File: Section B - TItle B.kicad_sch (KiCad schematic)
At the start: 20 parts, among them J2 CAN1, J5 RJHSE5380, J6 CAN1, U2 MCP2515-xST, U3 ISO1050DUB, U4 ISO1050DUB, Y1 ABM3B-8.000MHZ-10-1-U-T

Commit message: Final Changes, Updated to Checked
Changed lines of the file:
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@@
 		)
 	)
-	(text_box "Block Description"
+	(text_box "CAN1 - Native ESP32"
 		(exclude_from_sim no)
 		(at 129.54 80.01 0)
@@
 		(stroke
 			(width -0.0001)
-			(type default)
+			(type solid)
 		)
 		(fill
@@
 		)
 	)
-	(text_box "Block Description"
+	(text_box "CAN2 - Aux. CAN for Victron"
 		(exclude_from_sim no)
 		(at 129.54 133.35 0)
@@
 		(stroke
 			(width -0.0001)
-			(type default)
+			(type solid)
 		)
 		(fill
@@
 		)
 	)
-	(text_box "Block Description"
+	(text_box "Crystal for CAN"
 		(exclude_from_sim no)
 		(at 238.76 218.44 0)
@@
 		(stroke
 			(width -0.0001)
-			(type default)
+			(type solid)
 		)
 		(fill
@@
 		)
 	)
-	(text_box "Block Description"
+	(text_box "SPI CAN Interface"
 		(exclude_from_sim no)
 		(at 129.54 218.44 0)
@@
 		(stroke
 			(width -0.0001)
-			(type default)
+			(type solid)
 		)
 		(fill

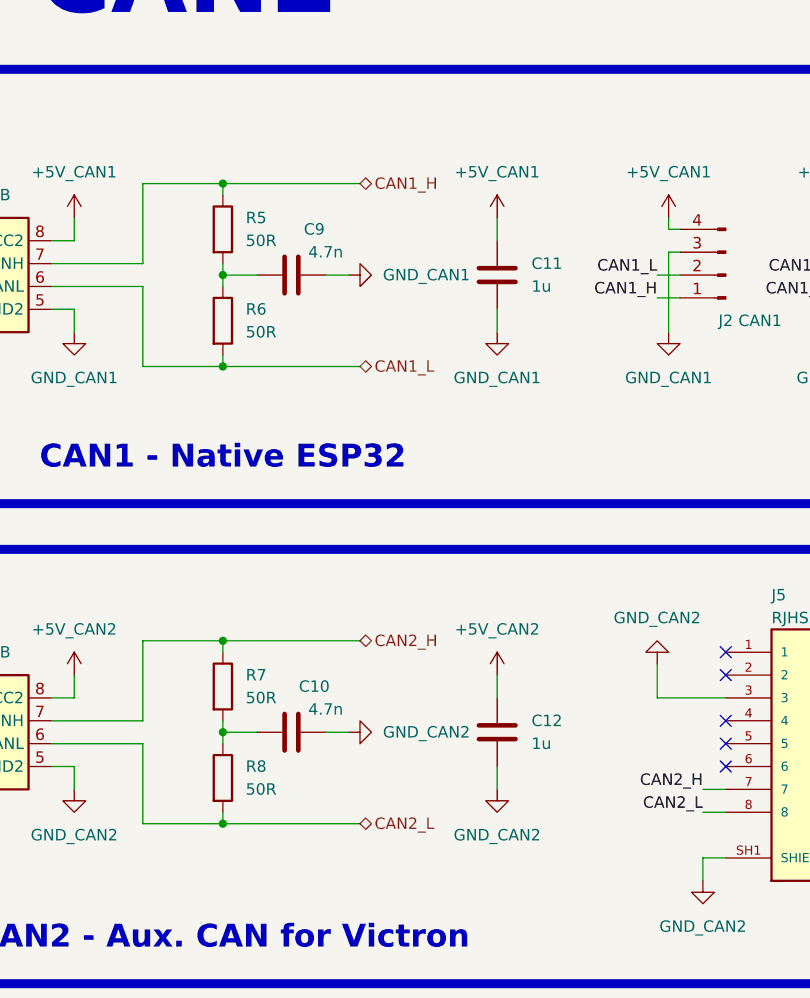
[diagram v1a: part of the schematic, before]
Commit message: Retry with rules DRC ERC passing
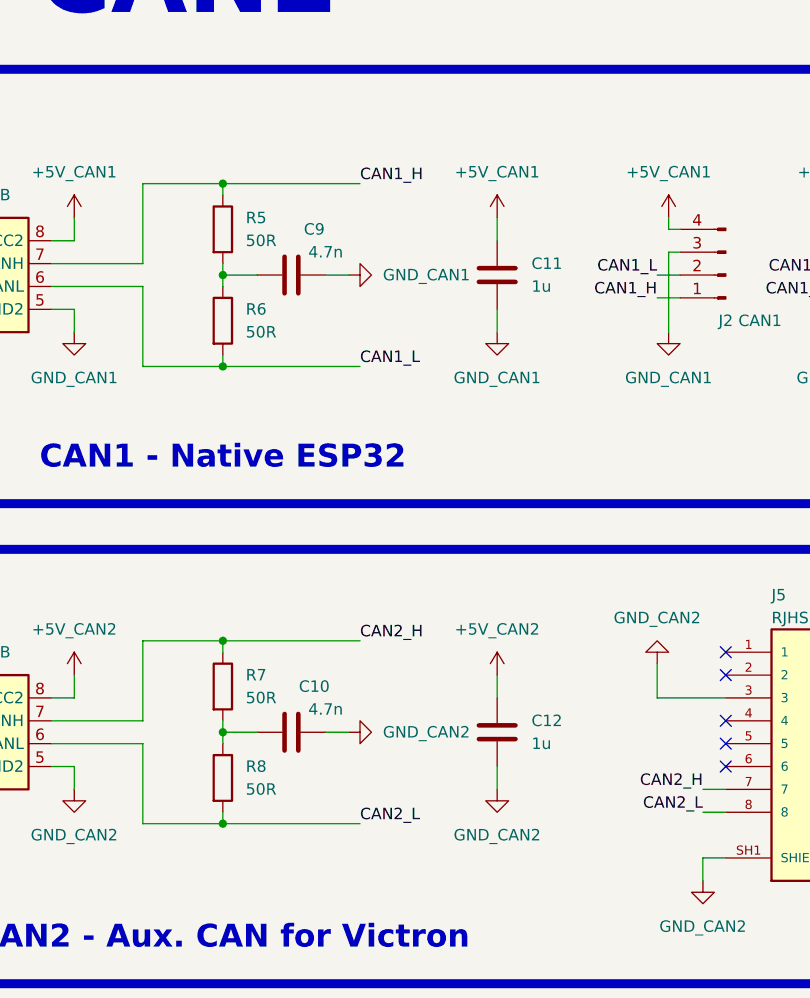
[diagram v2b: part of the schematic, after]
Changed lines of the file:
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@@
+		)
+	)
+	(label "CAN1_L"
+		(at 228.6 76.2 0)
+		(effects
+			(font
+				(size 1.27 1.27)
+			)
+			(justify left bottom)
 		)
 	)
@@
 		)
 	)
+	(label "CAN1_H"
+		(at 228.6 55.88 0)
+		(effects
+			(font
+				(size 1.27 1.27)
+			)
+			(justify left bottom)
+		)
+	)
 	(label "CAN2_H"
 		(at 266.7 123.19 180)
@@
 		)
 	)
+	(label "CAN2_H"
+		(at 228.6 106.68 0)
+		(effects
+			(font
+				(size 1.27 1.27)
+			)
+			(justify left bottom)
+		)
+	)
 	(label "CAN2_L"
 		(at 266.7 125.73 180)
@@
 			)
 			(justify right bottom)
+		)
+	)
+	(label "CAN2_L"
+		(at 228.6 127 0)
+		(effects
+			(font
+				(size 1.27 1.27)
+			)
+			(justify left bottom)
 		)
 	)
@@
 		)
 	)
-	(hierarchical_label "CAN2_L"
-		(shape bidirectional)
-		(at 228.6 127 0)
-		(effects
-			(font
-				(size 1.27 1.27)
-			)
-			(justify left)
-		)
-	)
-	(hierarchical_label "CAN1_L"
-		(shape bidirectional)
-		(at 228.6 76.2 0)
-		(effects
-			(font
-				(size 1.27 1.27)
-			)
-			(justify left)
-		)
-	)
-	(hierarchical_label "CAN2_H"
-		(shape bidirectional)
-		(at 228.6 106.68 0)
-		(effects
-			(font
-				(size 1.27 1.27)
-			)
-			(justify left)
-		)
-	)
 	(hierarchical_label "CAN2_INT"
 		(shape output)
@@
 		)
 	)
-	(hierarchical_label "CAN1_H"
-		(shape bidirectional)
-		(at 228.6 55.88 0)
-		(effects
-			(font
-				(size 1.27 1.27)
-			)
-			(justify left)
-		)
-	)
